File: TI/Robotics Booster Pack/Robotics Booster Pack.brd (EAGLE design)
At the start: 71.1 x 67.3 mm, 83 parts, among them U1 TPS62177.DQC, U11 SCHA4B0400, U13 XBEE-1XBEE-1_LOCK, U14 TPS5450, U3 DRV8800, U4 DRV8800, U5 DRV8800, U6 DRV8800, U7 PCA9557.RGV, U8 MPU-6050, U9 INA220.DGS

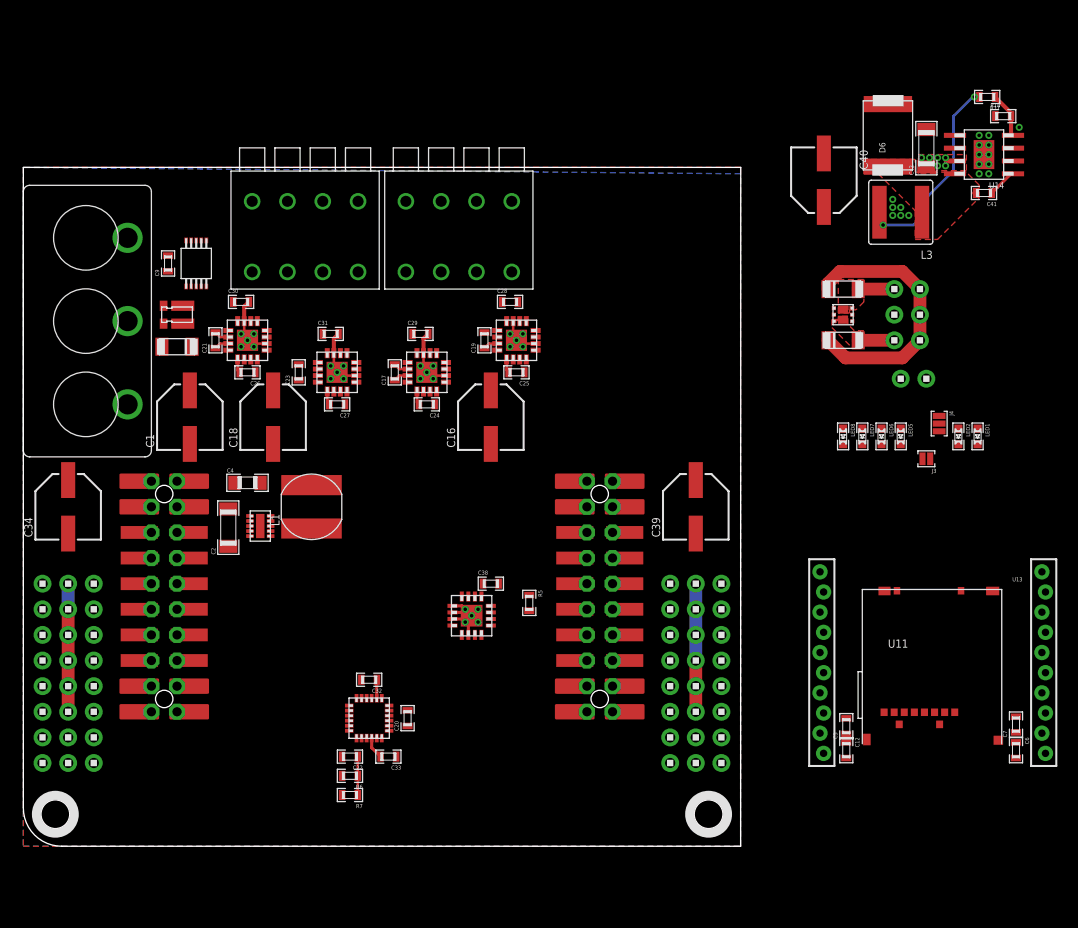
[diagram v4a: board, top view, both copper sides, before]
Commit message: Continuing RBP v3 rerouting. Figured out desired placement of headers. Thinking of adding FET to control power going out of board (NTMFS4897NFT1G). Need to replace IO expander; might need 16 pins instead of 8. Already running low on space...
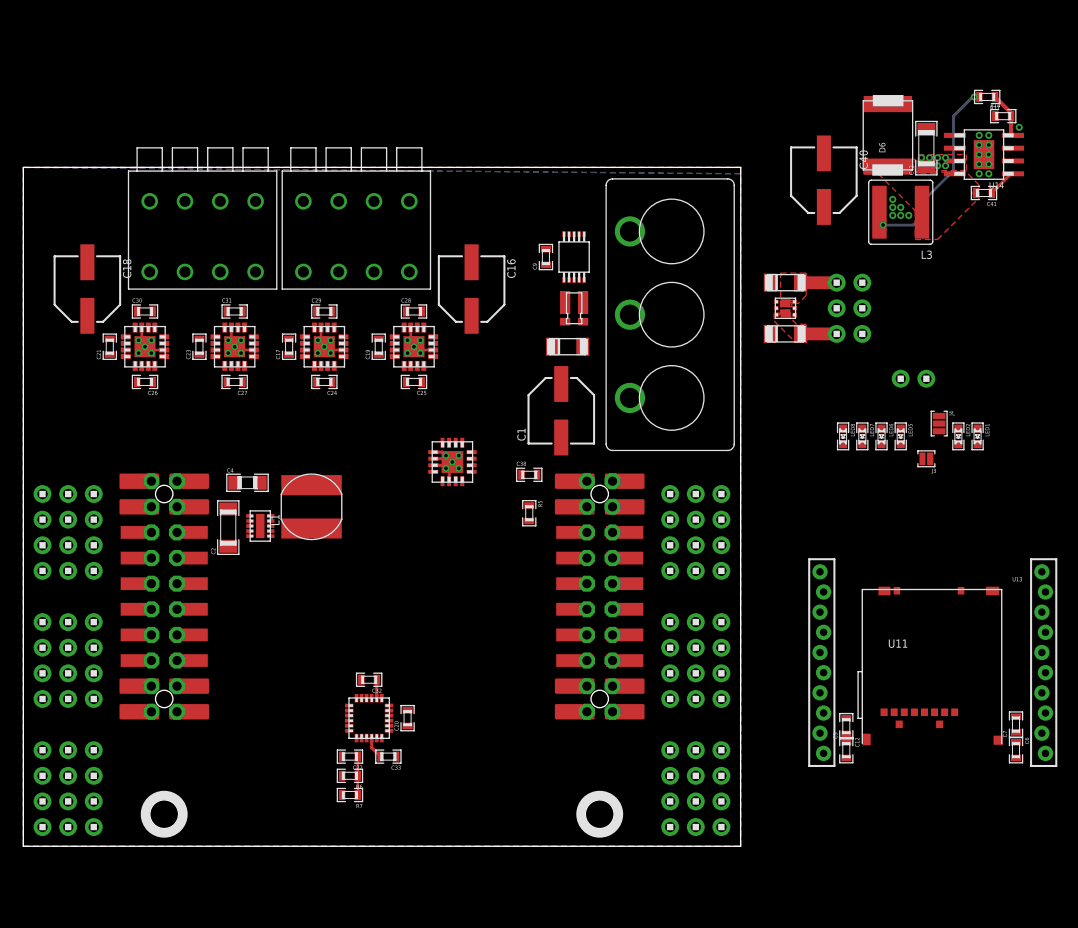
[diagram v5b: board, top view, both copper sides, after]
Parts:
- removed C34: 100uF, microbuilder:PANASONIC_D
- removed C39: 220uF, microbuilder:PANASONIC_D
- removed H13, H14: 2X3, headers(.1in):2X3
- added H16, H17, H18, H19, H20, H21, H22, H23, H25, H26, H27, H28: 1X4, headers(.1in):1X4
- H1, H2, H3, H4, H5, H6: value 1X6 -> 1X4; device headers(.1in):1X6 -> headers(.1in):1X4
- moved H1 62.9 mm to (6.99, 34.9)
- moved H3 62.9 mm to (1.91, 34.9)
- moved H2 62.9 mm to (4.45, 34.9)
- moved H11 45.1 mm to (57.8, 52.7), turned to 270 degrees
- moved R1 39.4 mm to (54.6, 53.3), turned to 270 degrees
- moved D1 38.7 mm to (54.0, 49.5), turned to 0 degrees
- moved C9 37.5 mm to (51.8, 58.4)
- moved U9 37.5 mm to (54.6, 58.4)
- moved C1 36.8 mm to (53.3, 43.2)
- moved C18 22.4 mm to (6.35, 55.2), turned to 270 degrees
- moved U7 15.4 mm to (42.5, 38.1)
- moved C16 12.8 mm to (44.5, 55.2), turned to 270 degrees
- moved C38 11.4 mm to (50.2, 36.8)
- moved U$3 10.8 mm to (14.0, 3.17)
- moved U$4 10.8 mm to (57.1, 3.17)
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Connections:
- removed net VSERVO: C39.+, H2.1, H2.2, H2.3, H2.4, H2.5, H2.6
- new net N$12: H12.9
- new net N$15: H12.11
- new net N$16: H12.13
- new net N$17: H12.15
- new net N$2: H12.1
- new net N$23: H12.17
- new net N$26: H12.19
- new net N$28: H12.20
- new net N$3: H12.3
- new net N$30: H12.18
- new net N$31: H12.16
- new net N$32: H12.14
- new net N$36: H12.12
- new net N$41: H12.10
- new net N$42: H12.8
- new net N$43: H12.6
- new net N$44: H12.4
- new net N$45: H12.2
- new net N$46: H15.1
- new net N$47: H15.3
- new net N$48: H15.5
- new net N$49: H15.7
- new net N$50: H15.9
- new net N$51: H15.11
- new net N$52: H15.13
- new net N$53: H15.15
- new net N$54: H15.17
- new net N$55: H15.19
- new net N$56: H15.20
- new net N$57: H15.18
- new net N$58: H15.16
- new net N$59: H15.14
- new net N$6: H12.7
- new net N$60: H15.12
- new net N$61: H15.10
- new net N$62: H15.8
- new net N$63: H15.6
- new net N$64: H15.4
- new net N$65: H15.2
- new net N$66: H20.1, H20.2, H20.3, H20.4
- new net N$67: H23.1, H23.2, H23.3, H23.4
- new net N$68: H27.1, H27.2, H27.3, H27.4
- new net N$69: H2.1, H2.2, H2.3, H2.4
- new net N$70: H5.1, H5.2, H5.3, H5.4
- new net N$71: H17.1, H17.2, H17.3, H17.4
- net 3.3V: no longer H13.3, H14.3
- net AD0: no longer H6.1
- net AD1: no longer H6.2
- net AD2: no longer H6.3
- net AD3: no longer H6.4
- net AD4: no longer H6.5
- net AD5: no longer H6.6
- net GND: now also H11.3, H18.1, H18.2, H18.3, H18.4, H21.1, H21.2, H21.3, H21.4, H25.1, H25.2, H25.3, H25.4, H28.1, H28.2, H28.3, H28.4, H3.1, H3.2, H3.3, H3.4, H6.1, H6.2, H6.3, H6.4; no longer C34.-, C39.-, H1.1, H1.2, H1.3, H1.4, H1.5, H1.6, H11.1, H13.1, H14.1, H4.1, H4.2, H4.3, H4.4, H4.5, H4.6
- net N$4: now also H12.5; no longer C34.+, H5.1, H5.2, H5.3, H5.4, H5.5, H5.6
- net QEI0.A: no longer H13.5
- net QEI0.B: no longer H13.6
- net QEI1.A: no longer H14.5
- net QEI1.B: no longer H14.6
- net SVRO0: no longer H3.1
- net SVRO1: no longer H3.2
- net SVRO2: no longer H3.3
- net SVRO3: no longer H3.4
- net SVRO4: no longer H3.5
- net SVRO5: no longer H3.6
- net VBAT: now also H11.1; no longer H11.3
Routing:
- net VFET: track 26.5 -> 0.00 mm
- net VSERVO: track 12.7 -> 0.00 mm
- net N$4: track 12.7 -> 0.00 mm
- net GND: track 29.5 -> 23.1 mm
- net N$27: track 1.46 -> 0.00 mm
- net N$38: track 1.46 -> 0.00 mm
- net N$25: track 1.46 -> 0.00 mm
- net N$37: track 1.46 -> 0.00 mm
- net N$13: track 1.46 -> 0.00 mm
- net N$21: track 1.36 -> 0.00 mm
- net N$18: track 1.36 -> 0.00 mm
- net N$20: track 1.36 -> 0.00 mm
- net N$19: track 1.36 -> 0.00 mm
- removed copper zone on layer 1, net N$4
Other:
- outline, holes or cut-outs redrawn

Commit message: Got everything mostly figured out as to where I want things. Using larger capacitors. Pin header mappings decided on. Routing will be hell... Still need to figure out how to distribute all power variants (3.3, 5v, Vin) to all header blocks (3.3v for signals, 5v for signals/servos, Vin for servo overvolting)
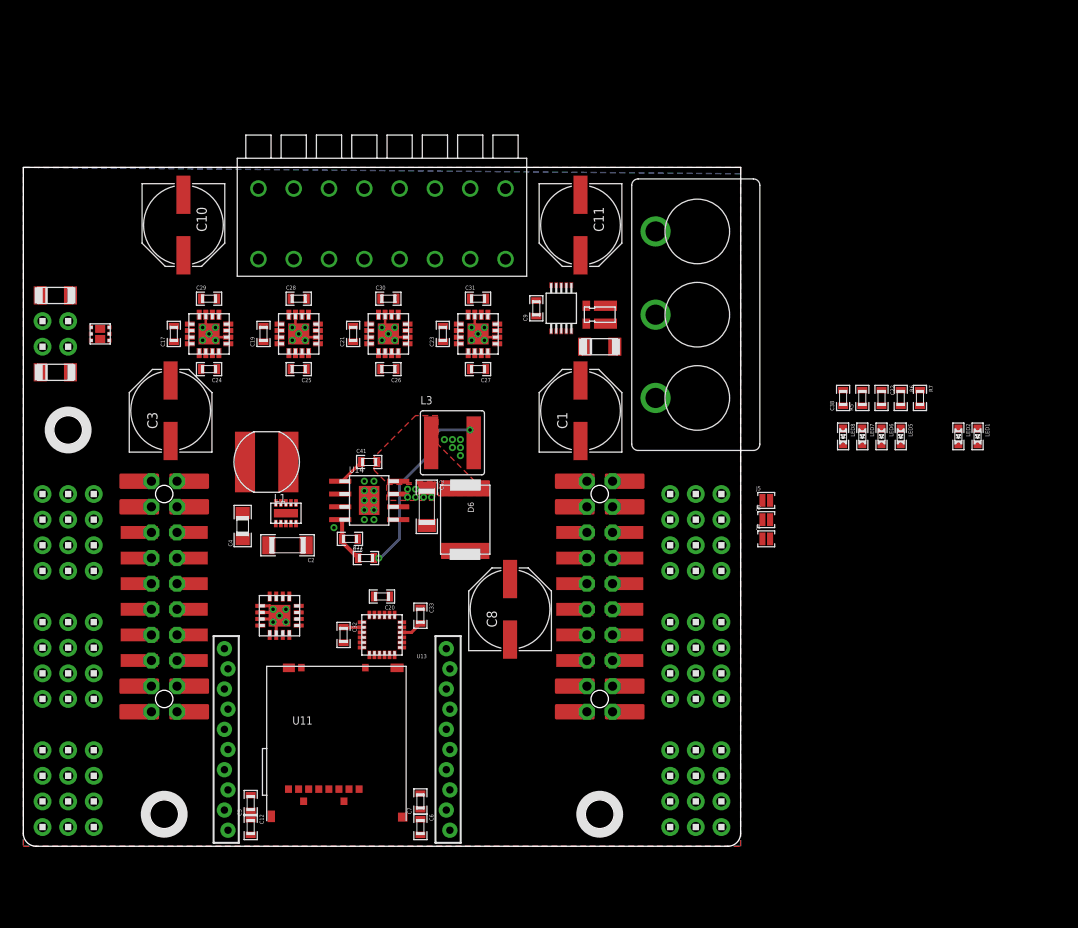
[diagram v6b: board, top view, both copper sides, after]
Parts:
- removed C16, C18: 47uF, microbuilder:PANASONIC_D
- removed C40: 330uF, microbuilder:PANASONIC_D
- removed H21, H27, H28: 1X4, headers(.1in):1X4
- removed H24: 1X2, headers(.1in):1X2
- removed J3: (no value), solderjumper:2.LRG
- removed J4: (no value), solderjumper:3.LRG.23
- added C10, C11, C3, C8: (no value), adafruit:PANASONIC_E
- added H30: 2X10.TSM-D-A, headers(.1in)(samtec):TSM-110-XX-XXX-DV-A
- added H31: 1X3.4DB, te-connectivity:4DB-P108-02
- added J1, J2, J5: (no value), solderjumper:2.LRG
- added U$21: HOLE.4MM, screw_holes:4MM
- C1: value 100uF -> (none); device microbuilder:PANASONIC_D -> adafruit:PANASONIC_E
- H10, H8: value 1X4.182440000 -> 1X4; device weidmuller:1824440000 -> headers(.1in):1X4
- H11: value 1X3.4DB -> 1X4; device te-connectivity:4DB-P108-02 -> headers(.1in):1X4
- H12, H15: value 2X10.TSM-D-A -> 1X4; device headers(.1in)(samtec):TSM-110-XX-XXX-DV-A -> headers(.1in):1X4
- H19, H20: value 1X4 -> 1X2; device headers(.1in):1X4 -> headers(.1in):1X2
- H25: value 1X4 -> 2X10.TSM-D-A; device headers(.1in):1X4 -> headers(.1in)(samtec):TSM-110-XX-XXX-DV-A
- H26: value 1X4 -> 1X8; device headers(.1in):1X4 -> weidmuller:1824480000
- H7, H9: value 1X3 -> 1X4; device headers(.1in):1X3 -> headers(.1in):1X4
- moved H9 91.4 mm to (1.91, 9.53)
- moved H7 86.7 mm to (6.99, 9.53), turned to 270 degrees
- moved R18 77.1 mm to (32.4, 30.5), turned to 180 degrees
- moved R17 76.7 mm to (34.0, 28.6), turned to 0 degrees
- moved D3 72.9 mm to (3.17, 47.0)
- moved D4 72.5 mm to (3.17, 54.6)
- moved U14 69.9 mm to (34.3, 34.3), turned to 0 degrees
- moved R7 68.9 mm to (88.9, 44.5), turned to 270 degrees
- moved Q1 68.0 mm to (7.62, 50.8), turned to 90 degrees
- moved H18 67.7 mm to (69.2, 1.91), turned to 90 degrees
- moved C41 66.5 mm to (34.3, 38.1), turned to 0 degrees
- moved R6 66.2 mm to (87.0, 44.5), turned to 270 degrees
- moved H19 66.1 mm to (1.91, 49.5)
- moved H20 66.1 mm to (4.45, 49.5)
- moved C22 63.6 mm to (85.1, 44.5), turned to 270 degrees
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- renumbered H22 to H13, H23 to H14
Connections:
- removed net N$12: H12.9
- removed net N$15: H12.11
- removed net N$16: H12.13
- removed net N$17: H12.15
- removed net N$2: H12.1
- removed net N$23: H12.17
- removed net N$26: H12.19
- removed net N$28: H12.20
- removed net N$3: H12.3
- removed net N$30: H12.18
- removed net N$31: H12.16
- removed net N$32: H12.14
- removed net N$36: H12.12
- removed net N$4: H12.5
- removed net N$41: H12.10
- removed net N$42: H12.8
- removed net N$43: H12.6
- removed net N$44: H12.4
- removed net N$45: H12.2
- removed net N$46: H15.1
- removed net N$47: H15.3
- removed net N$48: H15.5
- removed net N$49: H15.7
- removed net N$50: H15.9
- removed net N$51: H15.11
- removed net N$52: H15.13
- removed net N$53: H15.15
- removed net N$54: H15.17
- removed net N$55: H15.19
- removed net N$56: H15.20
- removed net N$57: H15.18
- removed net N$58: H15.16
- removed net N$59: H15.14
- removed net N$6: H12.7
- removed net N$60: H15.12
- removed net N$61: H15.10
- removed net N$62: H15.8
- removed net N$63: H15.6
- removed net N$64: H15.4
- removed net N$65: H15.2
- removed net N$68 (its old number): H27.1, H27.2, H27.3, H27.4
- removed net VDD: J4.2
- new net N$71: H8.1, H8.2, H8.3, H8.4
- new net N$72: C10.+, C28.1, C29.1, U5.8, U6.8
- new net N$73: C11.+, C30.1, C31.1, U3.8, U4.8
- new net PA2: H25.20, H7.1
- new net PA3: H25.18, H7.2
- new net PA4: H25.16, H7.3
- new net PA5: H30.15, H7.4
- new net PA6: H30.17, H4.3
- new net PA7: H30.19, H4.4
- new net PB0: H30.5
- new net PB1: H30.7
- new net PB2: H25.4
- new net PB3: H25.5
- new net PB4: H10.3, H30.13
- new net PB5: H10.4, H30.3
- new net PB6: H10.1, H25.14
- new net PB7: H10.2, H25.12
- new net PC4: H25.7
- new net PC5: H16.3, H25.9
- new net PC6: H16.4, H25.11
- new net PC7: H25.13
- new net PD0: H13.3, H30.6
- new net PD1: H13.4, H30.8
- new net PD2: H30.10, H4.2
- new net PD3: H30.12, H4.1
- new net PD6: H16.1, H25.15
- new net PD7: H16.2, H25.17
- new net PE0: H1.4, H25.6
- new net PE1: H1.3, H30.14
- new net PE2: H1.2, H30.16
- new net PE3: H1.1, H30.18
- new net PE4: H13.1, H30.9
- new net PE5: H13.2, H30.11
- new net PF0: H25.8
- new net PF1: H30.20
- new net PF2: H25.1
- new net PF3: H25.3
- new net PF4: H25.19
- net !RST: now also H25.10; no longer H24.1
- net 3.3V: now also H30.1
- net 5.0V: now also C8.+, H30.2; no longer C40.+, J4.3
- net FET0.D: now also H20.1; no longer H9.1
- net FET1.D: now also H20.2; no longer H9.3
- net GND: now also C10.-, C11.-, C8.-, H12.1, H12.2, H12.3, H12.4, H15.1, H15.2, H15.3, H15.4, H30.4, H31.3, H9.1, H9.3, H9.4; no longer C16.-, C18.-, C40.-, H11.3, H21.1, H21.2, H21.3, H21.4, H24.2, H25.1, H25.3, H25.4, H28.1, H28.2, H28.3, H28.4
- net M0+: now also H26.1@1, H26.1@2; no longer H8.1@1, H8.1@2
- net M0-: now also H26.2@1, H26.2@2; no longer H8.2@1, H8.2@2
- net M1+: now also H26.3@1, H26.3@2; no longer H8.3@1, H8.3@2
- net M1-: now also H26.4@1, H26.4@2; no longer H8.4@1, H8.4@2
- net M2+: now also H26.5@1, H26.5@2; no longer H10.1@1, H10.1@2
- net M2-: now also H26.6@1, H26.6@2; no longer H10.2@1, H10.2@2
- net M3+: now also H26.7@1, H26.7@2; no longer H10.3@1, H10.3@2
- net M3-: now also H26.8@1, H26.8@2; no longer H10.4@1, H10.4@2
- net N$22: now also H31.2; no longer H11.2
- net N$66: now also H11.1, H11.2, H11.3, H11.4; no longer H20.1, H20.2, H20.3, H20.4
- net VBAT: now also H31.1; no longer C16.+, C18.+, C28.1, C29.1, C30.1, C31.1, H11.1, J3.2, J4.1, U3.8, U4.8, U5.8, U6.8
- net VFET: now also H19.1, H19.2; no longer H7.1, H7.2, H7.3, J3.1
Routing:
- net 3.3V: track 3.81 -> 0.00 mm
- net FET1.D: track 3.58 -> 0.00 mm
- net FET0.D: track 3.58 -> 0.00 mm
- removed copper zone on layer 1, net FET0.D
- removed copper zone on layer 1, net FET1.D
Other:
- outline, holes or cut-outs redrawn
- board text added: "10"
- board text added: "11"
- board text added: "12"
- board text added: "13"
- board text added: "14"
- board text added: "15"
- board text added: "16"
- board text added: "17"
- board text added: "18"
- board text added: "19"
- board text added: "20"
- board text added: "21"
- board text added: "22"
- board text added: "23"
- board text added: "6"
- board text added: "7"
- board text added: "8"
- board text added: "9"
- board text removed: "FET"
- board text removed: "VFET"
